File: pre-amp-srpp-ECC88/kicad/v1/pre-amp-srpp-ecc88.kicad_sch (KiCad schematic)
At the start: 65 parts

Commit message: WIP
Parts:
- removed D1, D2: (no value), symbol Diode:1N4007
- removed R16, R17, R21, R22: (no value), symbol Device:R
- removed T1, T2: (no value), symbol w_vacuum:ECC88
- added U2, U3: ECC88, kicad-snk:TubeNoval-ECC88, symbol Valve:ECC88
- C1, C5: value (none) -> 3.3uF; footprint (none) -> Capacitor_THT:C_Rect_L7.2mm_W7.2mm_P5.00mm_FKS2_FKP2_MKS2_MKP2
- C10, C12, C3, C7: symbol pre-amp-ecc88-rescue:CP-Device -> Device:C_Polarized
- C11, C9: value (none) -> 100nF; footprint (none) -> Capacitor_THT:C_Rect_L7.2mm_W2.5mm_P5.00mm_FKS2_FKP2_MKS2_MKP2
- C13: value (none) -> 15uF/25V; footprint (none) -> Capacitor_Tantalum_SMD:CP_EIA-3216-12_Kemet-S_Pad1.58x1.35mm_HandSolder; symbol pre-amp-ecc88-rescue:CP-Device -> Device:C_Polarized
- C14, C15: value (none) -> 100nF/50V; footprint (none) -> Capacitor_SMD:C_0805_2012Metric_Pad1.18x1.45mm_HandSolder
- C2, C6: value (none) -> 100nF; footprint (none) -> Capacitor_THT:C_Rect_L16.5mm_W5.0mm_P15.00mm_MKT
- C4, C8: value (none) -> 2.2uF; footprint (none) -> Capacitor_THT:C_Rect_L31.5mm_W11.0mm_P27.50mm_MKS4
- D3, D4: value (none) -> 1N4148W; footprint (none) -> Diode_SMD:D_SOD-123
- H1, H2, H3, H4: value (none) -> MountingHole; footprint (none) -> MountingHole:MountingHole_3.2mm_M3
- J1, J11, J12, J2, J3, J4, J7, J8: value (none) -> Conn_01x01; footprint (none) -> Connector_Pin:Pin_D1.0mm_L10.0mm
- J10, J5, J6, J9: value (none) -> Conn_01x01; footprint (none) -> Connector_Pin:Pin_D1.3mm_L11.0mm
- K1: value (none) -> G6K-2; footprint (none) -> Relay_SMD:Relay_DPDT_Omron_G6K-2F-Y
- Q1: value (none) -> MMBT3904; footprint (none) -> Package_TO_SOT_SMD:SOT-23
- R1, R10, R18, R9: value (none) -> 1Meg; footprint (none) -> Resistor_SMD:R_MELF_MMB-0207
- R11, R2: value (none) -> 47k; footprint (none) -> Resistor_SMD:R_MELF_MMB-0207
- R12, R14: value (none) -> 50.1R; footprint (none) -> Resistor_SMD:R_MELF_MMB-0207
- R13, R8: value (none) -> 150R; footprint (none) -> Resistor_SMD:R_MELF_MMB-0207
- R15, R6: value (none) -> 100k; footprint (none) -> Resistor_SMD:R_MELF_MMB-0207
- R19: value (none) -> 2Meg; footprint (none) -> Resistor_SMD:R_0805_2012Metric_Pad1.20x1.40mm_HandSolder
- R20, R23: value (none) -> 2.49k; footprint (none) -> Resistor_SMD:R_0805_2012Metric_Pad1.20x1.40mm_HandSolder
- R24, R25: value (none) -> 470R; footprint (none) -> Resistor_SMD:R_MELF_MMB-0207
- R3, R4: value (none) -> 300R; footprint (none) -> Resistor_SMD:R_MELF_MMB-0207
- R5, R7: value (none) -> 200R; footprint (none) -> Resistor_SMD:R_MELF_MMB-0207
- U1: value (none) -> TLC555xD; footprint (none) -> Package_SO:SOIC-8_3.9x4.9mm_P1.27mm
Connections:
- net GND: now also R5.2; no longer C10.2, C11.2, C12.2, C14.2, C15.2, C9.2, D3.2 (A), J10.1 (Pin_1), Q1.2 (E), R12.2, R19.2, R23.2, R3.2, R8.2, U1.1 (GND)
- net VDDA: now also U2.6 (A), U3.6 (A); no longer R13.1, R14.1, R4.1, R5.1
- net at R4.2: now also U2.2 (G); no longer R5.2
- net at R2.1, R6.2: now also R4.1
- net at R3.1: now also R11.1, R15.2
- net at R13.2: now also C8.2, R14.1; no longer R14.2
- net at R12.1: now also C4.2, R8.2
- net VDDF renamed FVCC
- net FVCC: now also U2.5 (F2), U3.5 (F2)
- new net: R3.2, U3.2 (G)
- new net: R12.2, U2.1 (A), U2.7 (G)
- new net: R5.1, U2.3 (K)
- new net: R8.1, U2.8 (K)
- new net: R13.1, U3.8 (K)
- new net: R7.1, U3.3 (K)
- new net: R14.2, U3.1 (A), U3.7 (G)
- new net FGND: C10.2, C11.2, C12.2, C14.2, C15.2, C9.2, D3.2 (A), J10.1 (Pin_1), Q1.2 (E), R19.2, R23.2, U1.1 (GND), U2.4 (F1), U3.4 (F1)
- no-connect marks 1 -> 4
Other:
- title: Pre-Amp ECC88/E88CC -> SRPP+ Pre-Amp ECC88/E88CC
- moved on the sheet: C1, C10, C11, C12, C2, C3, C4, C5, C6, C7, C8, C9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

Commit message: Update
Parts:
- K1: value G6K-2 -> G6K-2F-TR DC6; footprint Relay_SMD:Relay_DPDT_Omron_G6K-2F-Y -> Relay_SMD:Relay_DPDT_Omron_G6K-2F
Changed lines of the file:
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@@
     (in_bom yes) (on_board yes)
     (property "Reference" "K1" (id 0) (at 281.1018 156.21 90))
-    (property "Value" "G6K-2" (id 1) (at 278.7904 156.21 90))
-    (property "Footprint" "Relay_SMD:Relay_DPDT_Omron_G6K-2F-Y" (id 2) (at 261.62 156.21 0)
+    (property "Value" "G6K-2F-TR DC6" (id 1) (at 278.7904 156.21 90))
+    (property "Footprint" "Relay_SMD:Relay_DPDT_Omron_G6K-2F" (id 2) (at 261.62 156.21 0)
       (effects (font (size 1.27 1.27)) (justify left) hide)
     )
@@
     )
     (path "/00000000-0000-0000-0000-0000606b8c32"
-      (reference "K1") (unit 1) (value "G6K-2") (footprint "Relay_SMD:Relay_DPDT_Omron_G6K-2F-Y")
+      (reference "K1") (unit 1) (value "G6K-2F-TR DC6") (footprint "Relay_SMD:Relay_DPDT_Omron_G6K-2F")
     )
     (path "/00000000-0000-0000-0000-0000606d875d"

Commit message: Update pre-amp-srpp-ecc88.kicad_sch
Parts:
- R11, R2: value 47k -> 10k
- R15, R6: value 100k -> 22k
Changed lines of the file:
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@@
   (title_block
     (title "SRPP+ Pre-Amp ECC88/E88CC")
-    (date "2022-08-13")
+    (date "2022-08-14")
     (rev "V1")
   )
@@
     (in_bom yes) (on_board yes)
     (property "Reference" "R2" (id 0) (at 81.28 69.0372 90))
-    (property "Value" "47k" (id 1) (at 81.28 71.3486 90))
+    (property "Value" "10k" (id 1) (at 81.28 71.3486 90))
     (property "Footprint" "Resistor_SMD:R_MELF_MMB-0207" (id 2) (at 81.28 72.517 90)
       (effects (font (size 1.27 1.27)) hide)
@@
     (in_bom yes) (on_board yes)
     (property "Reference" "R6" (id 0) (at 127 98.2472 90))
-    (property "Value" "100k" (id 1) (at 127 100.5586 90))
+    (property "Value" "22k" (id 1) (at 127 100.5586 90))
     (property "Footprint" "Resistor_SMD:R_MELF_MMB-0207" (id 2) (at 127 101.727 90)
       (effects (font (size 1.27 1.27)) hide)
@@
     (in_bom yes) (on_board yes)
     (property "Reference" "R11" (id 0) (at 81.28 164.2872 90))
-    (property "Value" "47k" (id 1) (at 81.28 166.5986 90))
+    (property "Value" "10k" (id 1) (at 81.28 166.5986 90))
     (property "Footprint" "Resistor_SMD:R_MELF_MMB-0207" (id 2) (at 81.28 167.767 90)
       (effects (font (size 1.27 1.27)) hide)
@@
     (in_bom yes) (on_board yes)
     (property "Reference" "R15" (id 0) (at 127 195.4022 90))
-    (property "Value" "100k" (id 1) (at 127 197.7136 90))
+    (property "Value" "22k" (id 1) (at 127 197.7136 90))
     (property "Footprint" "Resistor_SMD:R_MELF_MMB-0207" (id 2) (at 127 198.882 90)
       (effects (font (size 1.27 1.27)) hide)
@@
     )
     (path "/00000000-0000-0000-0000-000060068443"
-      (reference "R2") (unit 1) (value "47k") (footprint "Resistor_SMD:R_MELF_MMB-0207")
+      (reference "R2") (unit 1) (value "10k") (footprint "Resistor_SMD:R_MELF_MMB-0207")
     )
     (path "/1540f0d5-738c-46f4-ba14-b5592439796e"
@@
     )
     (path "/00000000-0000-0000-0000-00006007e95e"
-      (reference "R6") (unit 1) (value "100k") (footprint "Resistor_SMD:R_MELF_MMB-0207")
+      (reference "R6") (unit 1) (value "22k") (footprint "Resistor_SMD:R_MELF_MMB-0207")
     )
     (path "/655c3dc9-9ad3-4836-a093-dc6d055db80f"
@@
     )
     (path "/00000000-0000-0000-0000-00006010b707"
-      (reference "R11") (unit 1) (value "47k") (footprint "Resistor_SMD:R_MELF_MMB-0207")
+      (reference "R11") (unit 1) (value "10k") (footprint "Resistor_SMD:R_MELF_MMB-0207")
     )
     (path "/e60fd313-c765-402c-bb62-144469d3ec61"
@@
     )
     (path "/00000000-0000-0000-0000-00006010b789"
-      (reference "R15") (unit 1) (value "100k") (footprint "Resistor_SMD:R_MELF_MMB-0207")
+      (reference "R15") (unit 1) (value "22k") (footprint "Resistor_SMD:R_MELF_MMB-0207")
     )
     (path "/00000000-0000-0000-0000-00006010b775"

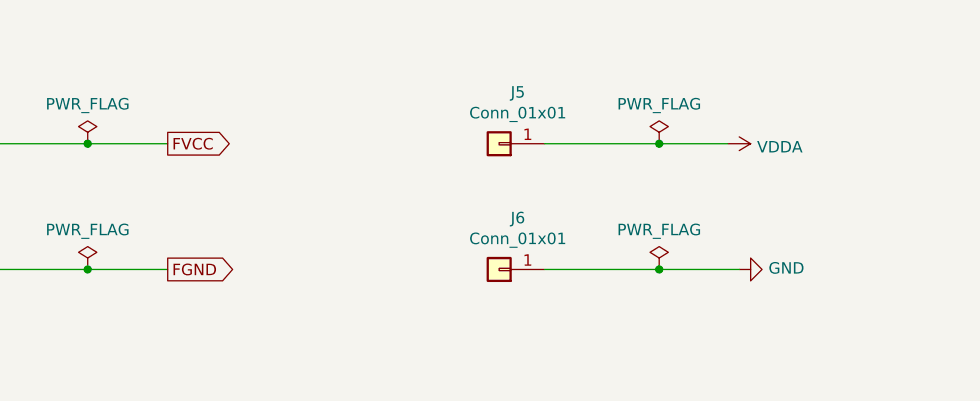
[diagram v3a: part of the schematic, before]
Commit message: Add voltage values
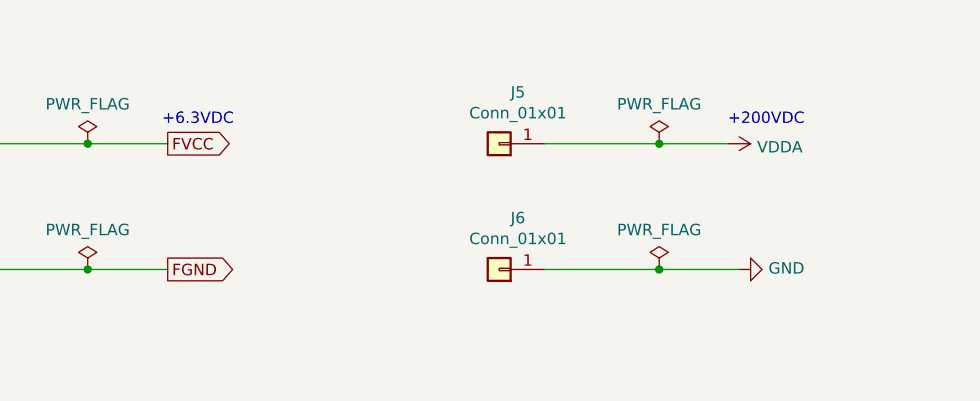
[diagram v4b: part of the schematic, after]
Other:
- note added: "+200VDC"
- note added: "+6.3VDC"
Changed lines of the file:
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@@
     (stroke (width 0) (type default) (color 0 0 0 0))
+  )
+  (text "+6.3VDC" (at 240.665 27.305 0)
+    (effects (font (size 1.27 1.27)) (justify left bottom))
+  )
+  (text "+200VDC" (at 303.53 27.305 0)
+    (effects (font (size 1.27 1.27)) (justify left bottom))
   )
   (global_label "FGND" (shape output) (at 241.3 43.18 0) (fields_autoplaced)
